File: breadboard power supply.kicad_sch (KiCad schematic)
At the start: 1 part

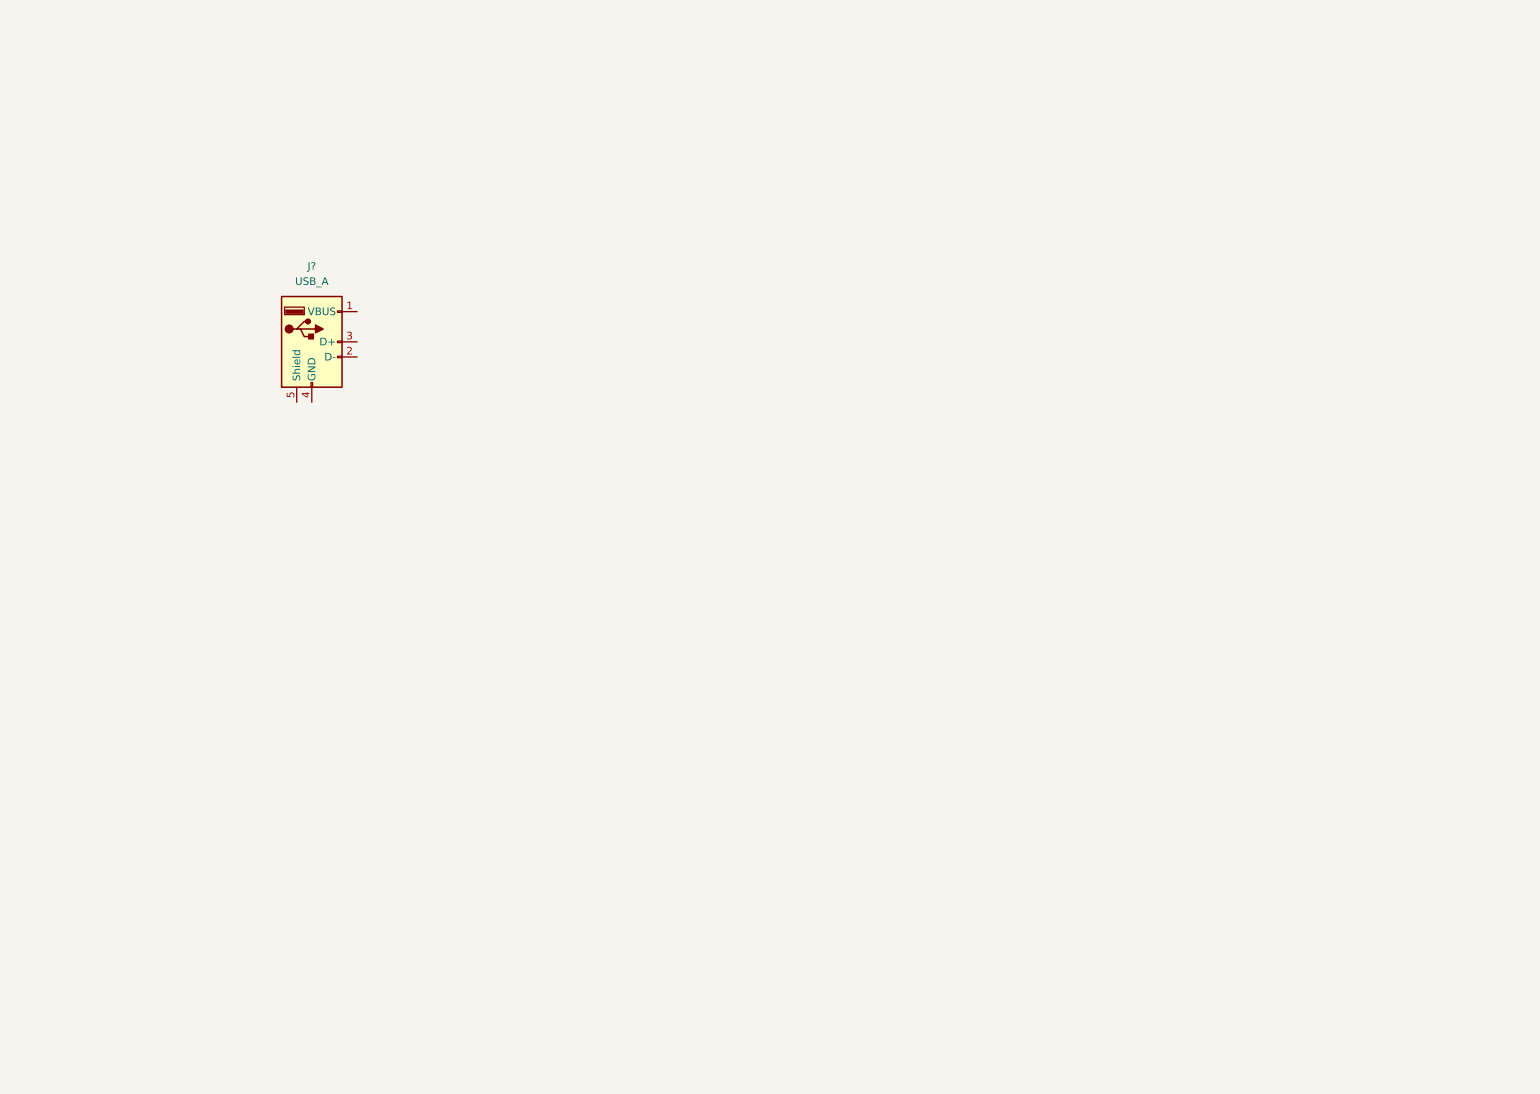
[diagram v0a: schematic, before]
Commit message: wiring done for schematic with usb, barrel jack and screw terminal as power input. values yet to assign
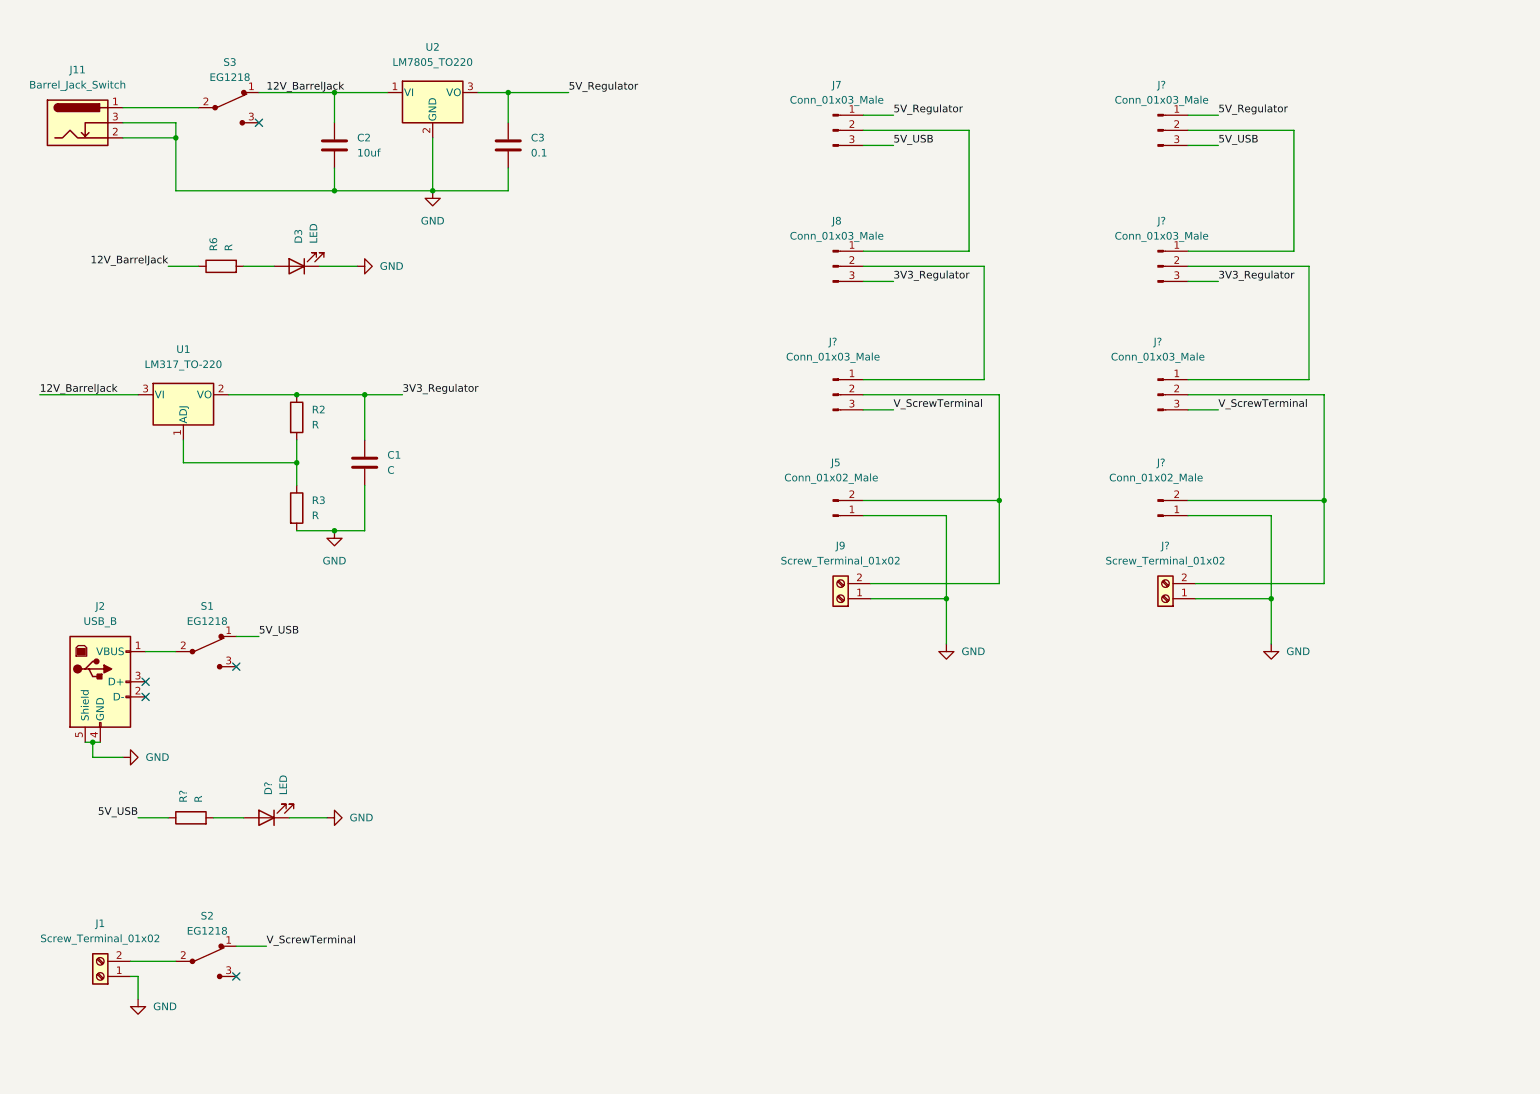
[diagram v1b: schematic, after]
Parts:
- removed J?: USB_A, symbol Connector:USB_A
- added C1: C, symbol Device:C
- added C2: 10uf, symbol Device:C
- added C3: 0.1, symbol Device:C
- added D3, D?: LED, symbol Device:LED
- added J1, J9, J?: Screw_Terminal_01x02, symbol Connector:Screw_Terminal_01x02
- added J11: Barrel_Jack_Switch, symbol Connector:Barrel_Jack_Switch
- added J2: USB_B, symbol Connector:USB_B
- added J5, J?: Conn_01x02_Male, symbol Connector:Conn_01x02_Male
- added J7, J8, J? (x4): Conn_01x03_Male, symbol Connector:Conn_01x03_Male
- added R2, R3, R6, R?: R, symbol Device:R
- added S1, S2, S3: EG1218, digikey-footprints:Switch_Slide_11.6x4mm_EG1218, symbol dk_Slide-Switches:EG1218
- added U1: LM317_TO-220, Package_TO_SOT_THT:TO-220-3_Vertical, symbol Regulator_Linear:LM317_TO-220
- added U2: LM7805_TO220, Package_TO_SOT_THT:TO-220-3_Vertical, symbol Regulator_Linear:LM7805_TO220
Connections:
- new net: J?.1 (Pin_1), J?.2 (Pin_2) (x2)
- new net: J?.2 (Pin_2), J?.2 (Pin_2), J?.2 (Pin_2)
- new net: J7.2 (Pin_2), J8.1 (Pin_1)
- new net: J8.2 (Pin_2), J?.1 (Pin_1)
- new net: R2.2, R3.1, U1.1 (ADJ)
- new net: D3.2 (A), R6.2
- new net: J5.2 (Pin_2), J9.2 (Pin_2), J?.2 (Pin_2)
- new net: J11.1, S3.2
- new net: J1.2 (Pin_2), S2.2
- new net: J2.1 (VBUS), S1.2
- new net: D?.2 (A), R?.2
- new net 12V_BarrelJack: C2.1, R6.1, S3.1, U1.3 (VI), U2.1 (VI)
- new net 3V3_Regulator: C1.1, J8.3 (Pin_3), J?.3 (Pin_3), R2.1, U1.2 (VO)
- new net 5V_Regulator: C3.1, J7.1 (Pin_1), J?.1 (Pin_1), U2.3 (VO)
- new net 5V_USB: J7.3 (Pin_3), J?.3 (Pin_3), R?.1, S1.1
- new net GND: C1.2, C2.2, C3.2, D3.1 (K), D?.1 (K), J1.1 (Pin_1), J11.2, J11.3, J2.4 (GND), J2.5 (Shield), J5.1 (Pin_1), J9.1 (Pin_1), J?.1 (Pin_1), J?.1 (Pin_1), R3.2, U2.2 (GND)
- new net V_ScrewTerminal: J?.3 (Pin_3), J?.3 (Pin_3), S2.1
- no-connect marks 0 -> 5
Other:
- title: (none) -> Breadboard Power Supply

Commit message: values assigned. annotated. text added. ERC done, no error. footprint yet to assign
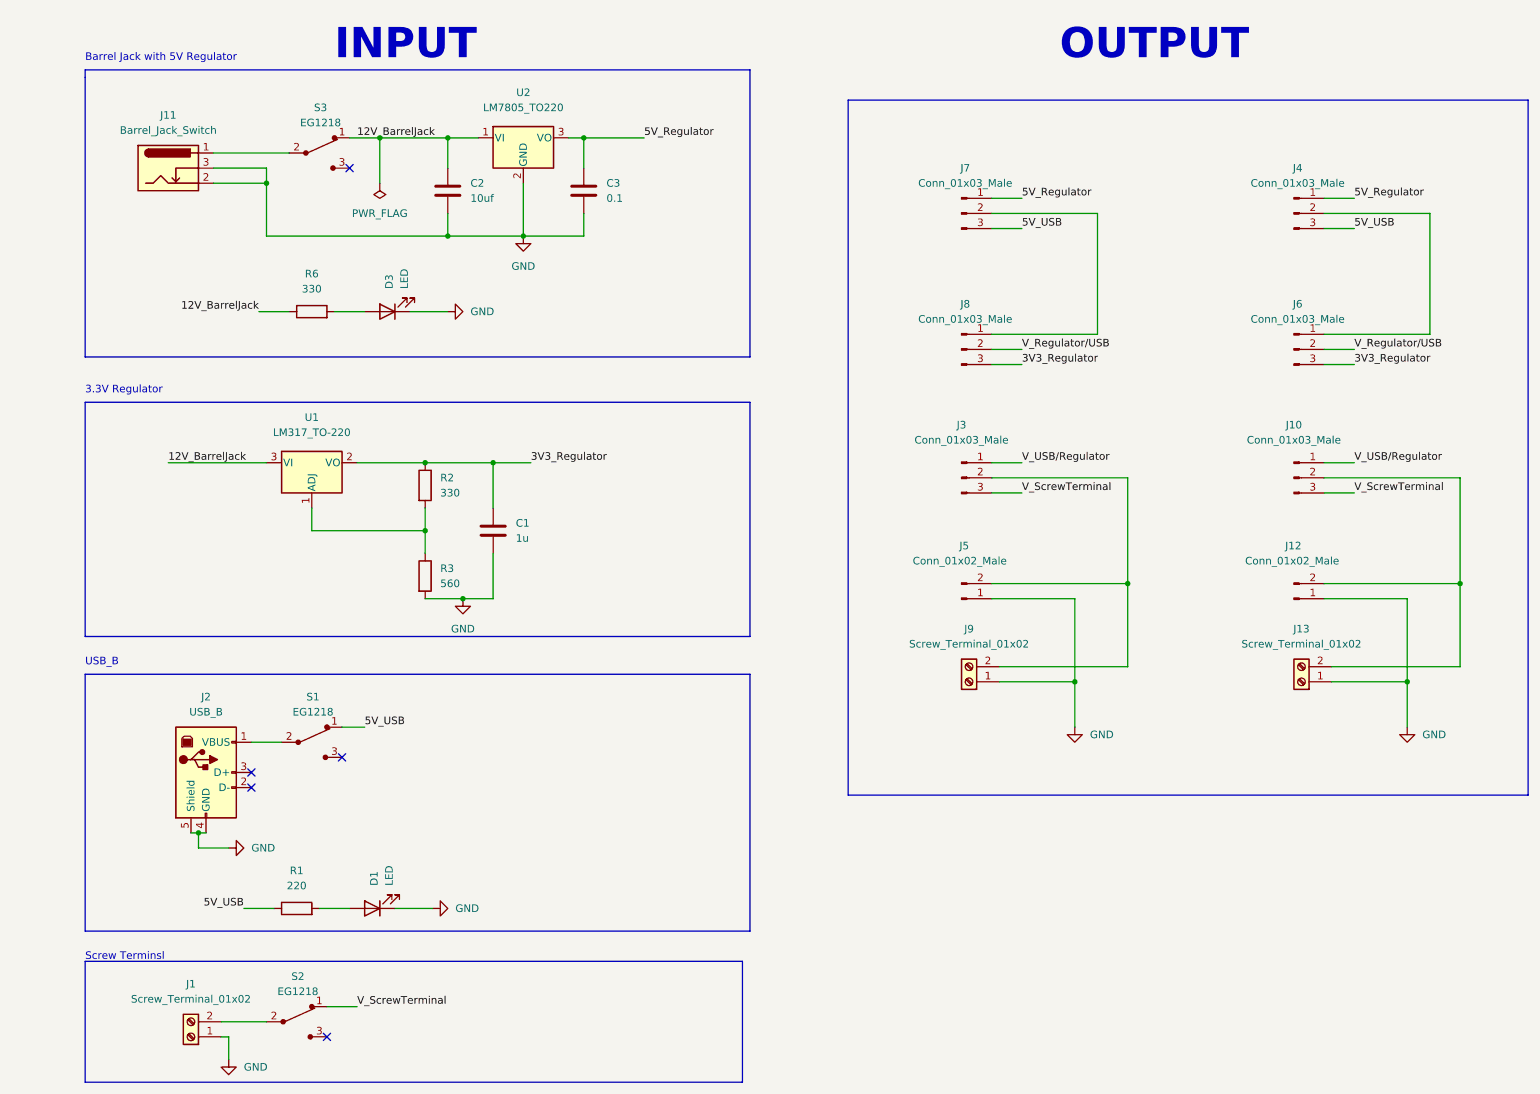
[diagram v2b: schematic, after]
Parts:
- removed J? (x3): Conn_01x03_Male, symbol Connector:Conn_01x03_Male
- removed J?: Conn_01x02_Male, symbol Connector:Conn_01x02_Male
- removed J?: Screw_Terminal_01x02, symbol Connector:Screw_Terminal_01x02
- added J10, J4, J6: Conn_01x03_Male, symbol Connector:Conn_01x03_Male
- added J12: Conn_01x02_Male, symbol Connector:Conn_01x02_Male
- added J13: Screw_Terminal_01x02, symbol Connector:Screw_Terminal_01x02
- C1: value C -> 1u
- R1: renamed from R?; value R -> 220
- R2, R6: value R -> 330
- R3: value R -> 560
- gave numbers to parts that had none: 2
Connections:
- net 3V3_Regulator: now also J6.3 (Pin_3)
- net 5V_Regulator: now also J4.1 (Pin_1)
- net 5V_USB: now also J4.3 (Pin_3)
- net GND: now also J12.1 (Pin_1), J13.1 (Pin_1)
- net V_ScrewTerminal: now also J10.3 (Pin_3)
- net V_Regulator/USB: now reaches J8.2 (Pin_2)
- net V_Regulator/USB: now also J6.2 (Pin_2); no longer J3.1 (Pin_1)
- new net: J4.2 (Pin_2), J6.1 (Pin_1)
- new net: J10.2 (Pin_2), J12.2 (Pin_2), J13.2 (Pin_2)
- new net V_USB/Regulator: J10.1 (Pin_1), J3.1 (Pin_1)
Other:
- note added: "3.3V Regulator"
- note added: "Barrel Jack with 5V Regulator"
- note added: "INPUT"
- note added: "OUTPUT"
- note added: "Screw Terminsl"
- note added: "USB_B"
- moved on the sheet: C1, C2, C3, D1, D3, J1, J11, J2, J3, J5, J7, J8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

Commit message: footprint assigned/associated
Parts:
- C1, C2, C3: footprint (none) -> Capacitor_THT:C_Disc_D3.0mm_W1.6mm_P2.50mm
- D1, D3: footprint (none) -> LED_THT:LED_D5.0mm
- J1, J13, J9: footprint (none) -> TerminalBlock:TerminalBlock_bornier-2_P5.08mm
- J10, J3, J4, J6, J7, J8: footprint (none) -> Connector_PinHeader_2.54mm:PinHeader_1x03_P2.54mm_Vertical
- J11: footprint (none) -> Connector_BarrelJack:BarrelJack_Horizontal
- J12, J5: footprint (none) -> Connector_PinHeader_2.54mm:PinHeader_1x02_P2.54mm_Vertical
- J2: footprint (none) -> Connector_USB:USB_B_Lumberg_2411_02_Horizontal
- R1, R2, R3, R6: footprint (none) -> Resistor_THT:R_Axial_DIN0204_L3.6mm_D1.6mm_P7.62mm_Horizontal

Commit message: board autorouted.
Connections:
- net V_USB/Regulator is gone; now on net V_Regulator/USB: J10.1 (Pin_1), J3.1 (Pin_1)
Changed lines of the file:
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@@
-    (effects (font (size 1.27 1.27)) (justify left bottom))
-  )
-  (label "V_USB{slash}Regulator" (at 186.69 88.9 0)
     (effects (font (size 1.27 1.27)) (justify left bottom))
   )
@@
     (effects (font (size 1.27 1.27)) (justify left bottom))
   )
-  (label "V_USB{slash}Regulator" (at 242.57 88.9 0)
+  (label "12V_BarrelJack" (at 43.18 88.9 0)
     (effects (font (size 1.27 1.27)) (justify left bottom))
   )
-  (label "12V_BarrelJack" (at 43.18 88.9 0)
+  (label "V_Regulator{slash}USB" (at 242.57 88.9 0)
     (effects (font (size 1.27 1.27)) (justify left bottom))
   )
@@
     (effects (font (size 1.27 1.27)) (justify left bottom))
   )
+  (label "V_Regulator{slash}USB" (at 186.69 88.9 0)
+    (effects (font (size 1.27 1.27)) (justify left bottom))
+  )
